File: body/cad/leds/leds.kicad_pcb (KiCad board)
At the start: 2 copper layers, 38 parts, among them J1 Conn_01x02, SW1 SW_DPST_x2

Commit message: optimze design, finalize layout
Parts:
- removed SW1: SW_DPST_x2, Buttons_Switches_ThroughHole:SW_DIP_x2_W7.62mm_Piano
- added J2: Conn_01x02, Pin_Headers:Pin_Header_Straight_1x02_Pitch2.54mm, F.Cu at (208.5, 111.3)
- moved D31 86.2 mm to (224.8, 64.8), turned to 270 degrees
- moved D32 83.7 mm to (226.1, 73.7), turned to 180 degrees
- moved D33 81.1 mm to (226.1, 81.3), turned to 180 degrees
- moved D34 79.2 mm to (226.1, 88.9), turned to 180 degrees
- moved D35 78.0 mm to (226.1, 96.5), turned to 180 degrees
- moved D36 76.3 mm to (224.8, 105.4), turned to 90 degrees
- moved J1 51.5 mm to (199.6, 111.3), turned to 90 degrees
- moved D1 1.80 mm to (186.7, 64.8), turned to 270 degrees
- moved D11 1.80 mm to (194.3, 64.8), turned to 270 degrees
- moved D17 1.80 mm to (201.9, 64.8), turned to 270 degrees
- moved D23 1.80 mm to (209.6, 64.8), turned to 270 degrees
- moved D12 1.80 mm to (194.3, 105.4), turned to 90 degrees
- moved D18 1.80 mm to (201.9, 105.4), turned to 90 degrees
- moved D24 1.80 mm to (209.6, 105.4), turned to 90 degrees
- moved D29 1.80 mm to (217.2, 64.8), turned to 270 degrees
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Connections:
- D1 pad 2: Net-(D1-Pad2) -> Wide_Circle
- D10 pad 2: Net-(D10-Pad2) -> Spott_Circle
- D11 pad 2: Net-(D1-Pad2) -> Wide_Circle
- D12 pad 2: Net-(D1-Pad2) -> Wide_Circle
- D13 pad 2: Net-(D10-Pad2) -> Spott_Circle
- D14 pad 2: Net-(D10-Pad2) -> Spott_Circle
- D15 pad 2: Net-(D10-Pad2) -> Spott_Circle
- D16 pad 2: Net-(D10-Pad2) -> Spott_Circle
- D17 pad 2: Net-(D1-Pad2) -> Wide_Circle
- D18 pad 2: Net-(D1-Pad2) -> Wide_Circle
- D19 pad 2: Net-(D10-Pad2) -> Spott_Circle
- D2 pad 2: Net-(D1-Pad2) -> Wide_Circle
- D20 pad 2: Net-(D10-Pad2) -> Spott_Circle
- D21 pad 2: Net-(D10-Pad2) -> Spott_Circle
- D22 pad 2: Net-(D10-Pad2) -> Spott_Circle
- D23 pad 2: Net-(D1-Pad2) -> Wide_Circle
- D24 pad 2: Net-(D1-Pad2) -> Wide_Circle
- D25 pad 2: Net-(D10-Pad2) -> Spott_Circle
- D26 pad 2: Net-(D10-Pad2) -> Spott_Circle
- D27 pad 2: Net-(D10-Pad2) -> Spott_Circle
- D28 pad 2: Net-(D10-Pad2) -> Spott_Circle
- D29 pad 2: Net-(D1-Pad2) -> Wide_Circle
- D3 pad 2: Net-(D1-Pad2) -> Wide_Circle
- D30 pad 2: Net-(D1-Pad2) -> Wide_Circle
- D31 pad 2: Net-(D1-Pad2) -> Wide_Circle
- D32 pad 2: Net-(D1-Pad2) -> Wide_Circle
- D33 pad 2: Net-(D1-Pad2) -> Wide_Circle
- D34 pad 2: Net-(D1-Pad2) -> Wide_Circle
- D35 pad 2: Net-(D1-Pad2) -> Wide_Circle
- D36 pad 2: Net-(D1-Pad2) -> Wide_Circle
- D4 pad 2: Net-(D1-Pad2) -> Wide_Circle
- D5 pad 2: Net-(D1-Pad2) -> Wide_Circle
- D6 pad 2: Net-(D1-Pad2) -> Wide_Circle
- D7 pad 2: Net-(D10-Pad2) -> Spott_Circle
- D8 pad 2: Net-(D10-Pad2) -> Spott_Circle
- D9 pad 2: Net-(D10-Pad2) -> Spott_Circle
- J1 pad 1: +3V8 -> Wide_Circle
- J1 pad 2: GND -> Spott_Circle
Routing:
- net GND: track 0.00 -> 303.5 mm
- net Wide_Circle: track 0.00 -> 158.7 mm
- net Spott_Circle: track 0.00 -> 141.9 mm, vias 0 -> 2
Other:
- net class Default: clearance 0.2 -> 0.5; trace_width 0.25 -> 1; via_dia 0.6 -> 1
- rule trace_clearance: 0.2 -> 0.5

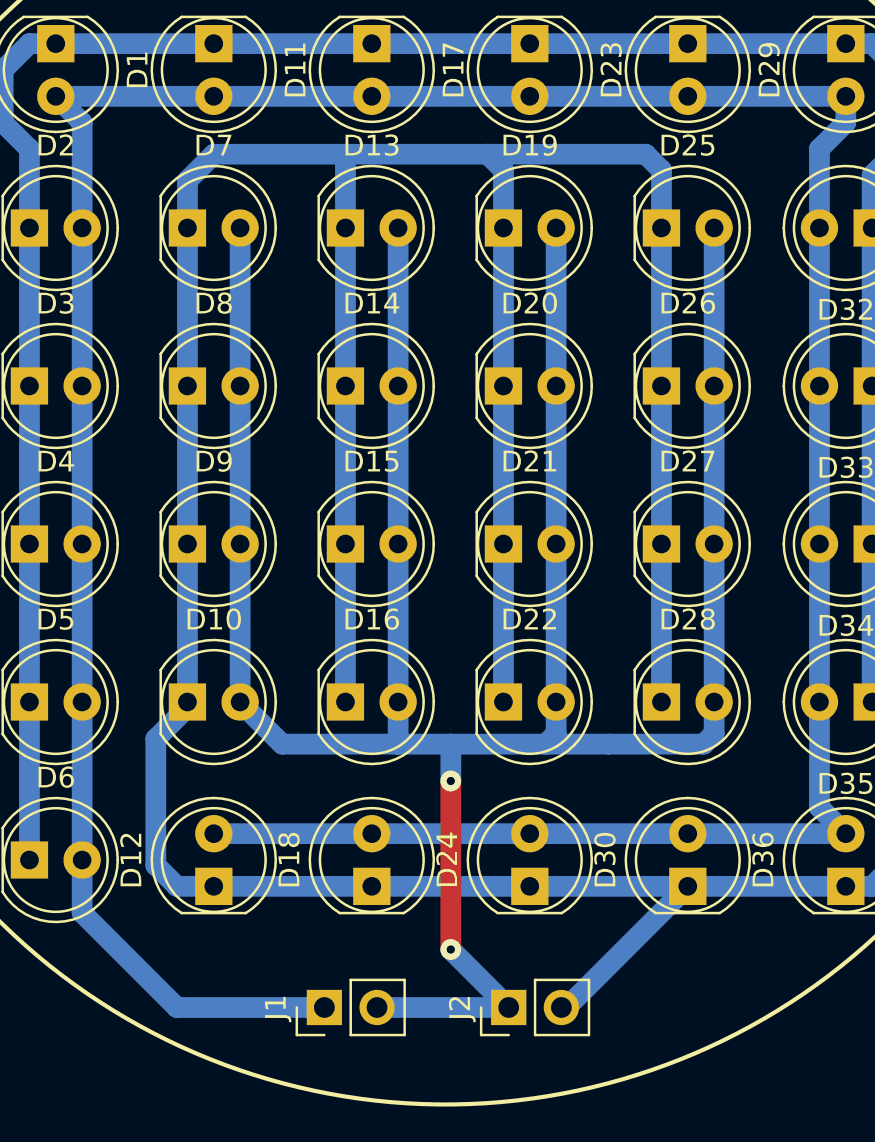
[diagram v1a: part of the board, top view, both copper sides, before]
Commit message: remove via
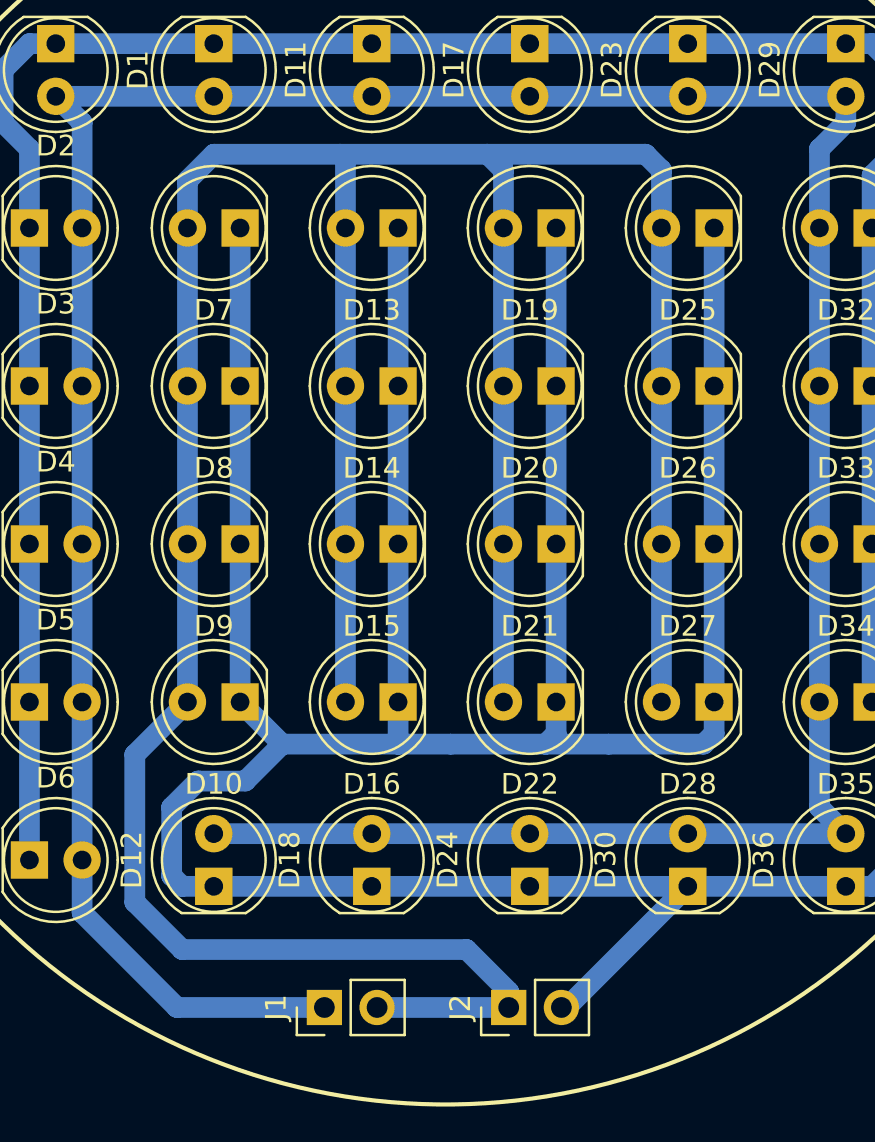
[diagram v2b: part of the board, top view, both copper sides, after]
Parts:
- moved D10 2.54 mm to (195.6, 96.5), turned to 180 degrees
- moved D7 2.54 mm to (195.6, 73.7), turned to 180 degrees
- moved D8 2.54 mm to (195.6, 81.3), turned to 180 degrees
- moved D9 2.54 mm to (195.6, 88.9), turned to 180 degrees
- moved D13 2.54 mm to (203.2, 73.7), turned to 180 degrees
- moved D14 2.54 mm to (203.2, 81.3), turned to 180 degrees
- moved D15 2.54 mm to (203.2, 88.9), turned to 180 degrees
- moved D16 2.54 mm to (203.2, 96.5), turned to 180 degrees
- moved D19 2.54 mm to (210.8, 73.7), turned to 180 degrees
- moved D20 2.54 mm to (210.8, 81.3), turned to 180 degrees
- moved D21 2.54 mm to (210.8, 88.9), turned to 180 degrees
- moved D22 2.54 mm to (210.8, 96.5), turned to 180 degrees
- moved D25 2.54 mm to (218.4, 73.7), turned to 180 degrees
- moved D26 2.54 mm to (218.4, 81.3), turned to 180 degrees
- moved D27 2.54 mm to (218.4, 88.9), turned to 180 degrees
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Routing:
- net Spott_Circle: track 141.9 -> 166.2 mm, vias 2 -> 0
- net GND: track 303.5 -> 297.4 mm
